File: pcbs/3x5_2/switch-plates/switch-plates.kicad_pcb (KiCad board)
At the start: 2 copper layers, 106.9 x 89.8 mm, 6 parts

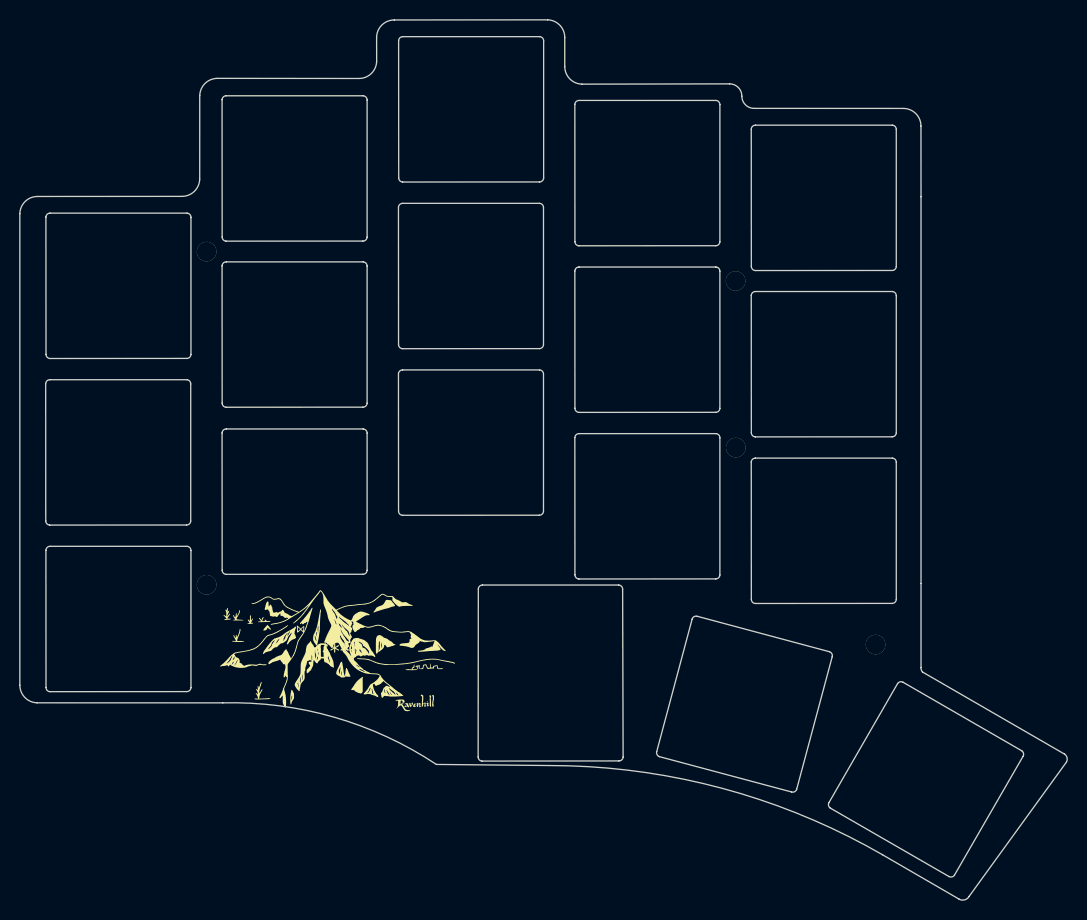
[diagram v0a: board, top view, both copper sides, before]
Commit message: redoing the switch plates cutouts and adding a proper kicad library
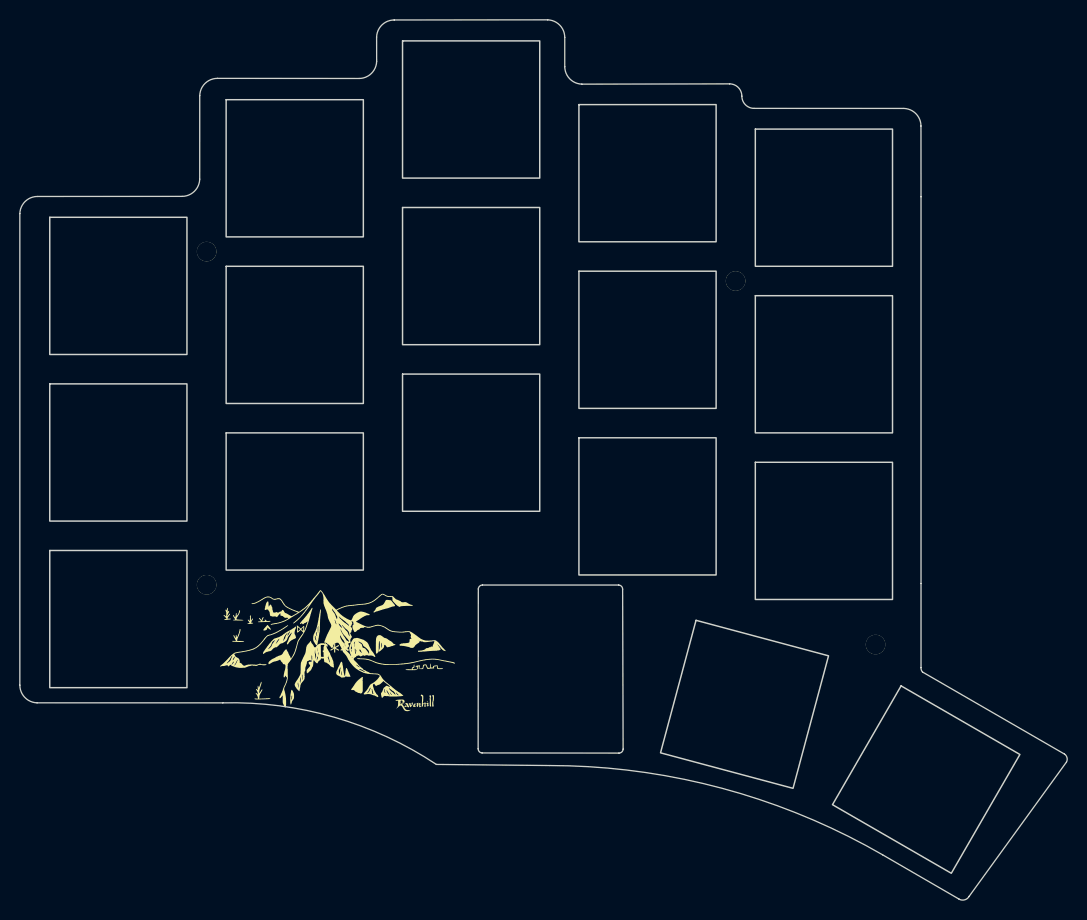
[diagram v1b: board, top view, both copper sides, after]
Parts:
- removed the ? at (134.2, 103.8)
- added SW1: Choc, arkenswoop:SW_PG1350_plate_cutout, F.Cu at (71.2, 87.2)
- added SW10: Choc, arkenswoop:SW_PG1350_plate_cutout, F.Cu at (143.2, 95.2)
- added SW11: Choc, arkenswoop:SW_PG1350_plate_cutout, F.Cu at (71.2, 121.2)
- added SW12: Choc, arkenswoop:SW_PG1350_plate_cutout, F.Cu at (89.2, 109.2)
- added SW13: Choc, arkenswoop:SW_PG1350_plate_cutout, F.Cu at (107.2, 103.2)
- added SW14: Choc, arkenswoop:SW_PG1350_plate_cutout, F.Cu at (125.2, 109.7)
- added SW15: Choc, arkenswoop:SW_PG1350_plate_cutout, F.Cu at (143.2, 112.2)
- added SW16: Choc, arkenswoop:SW_PG1350_plate_cutout, F.Cu at (135.1, 129.9)
- added SW17: Choc, arkenswoop:SW_PG1350_plate_cutout, F.Cu at (153.7, 137.6)
- added SW2: Choc, arkenswoop:SW_PG1350_plate_cutout, F.Cu at (89.2, 75.2)
- added SW3: Choc, arkenswoop:SW_PG1350_plate_cutout, F.Cu at (107.2, 69.2)
- added SW4: Choc, arkenswoop:SW_PG1350_plate_cutout, F.Cu at (125.2, 75.7)
- added SW5: Choc, arkenswoop:SW_PG1350_plate_cutout, F.Cu at (143.2, 78.2)
- added SW6: Choc, arkenswoop:SW_PG1350_plate_cutout, F.Cu at (71.2, 104.2)
- added SW7: Choc, arkenswoop:SW_PG1350_plate_cutout, F.Cu at (89.2, 92.2)
- added SW8: Choc, arkenswoop:SW_PG1350_plate_cutout, F.Cu at (107.2, 86.2)
- added SW9: Choc, arkenswoop:SW_PG1350_plate_cutout, F.Cu at (125.2, 92.7)
- ? (x4): value (none) -> M2_2mm_hole; footprint (none) -> arkenswoop:M2_2mm_hole
- G***: footprint Library:erebor_silk -> arkenswoop:erebor_silk
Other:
- outline, holes or cut-outs redrawn
